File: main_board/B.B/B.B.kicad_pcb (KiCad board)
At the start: 4 copper layers, 196 x 98 mm, 254 parts, among them J2 Conn_01x11, J3 Conn_01x11, J5 USB_C_Receptacle_USB2.0, M1 Motor_DC, Q1 2N7002, Q10 2N7002, Q11 SI3447CDV, Q2 2N7002, Q3 AO3400A, Q5 SI3447CDV, Q7 SI3447CDV, Q8 2N7002, Q9 SI3447CDV, SW1 SW_DIP_x01, SW2 SW_DIP_x01, SW3 SW_DIP_x01, SW4 SW_DIP_x02, U1 WS2812, U10 WS2812, U11 WS2812, U12 WS2812, U13 WS2812, U14 WS2812, U15 WS2812, U16 WS2812, U17 WS2812, U18 WS2812, U19 WS2812, U2 WS2812, U20 WS2812, U21 WS2812, U22 WS2812, U23 WS2812, U24 WS2812, U25 WS2812, U26 WS2812, U27 WS2812, U28 WS2812, U29 WS2812, U3 WS2812, U30 WS2812, U31 WS2812, U32 WS2812, U33 WS2812, U34 WS2812, U35 WS2812, U36 WS2812, U37 WS2812, U38 WS2812, U39 WS2812, U4 WS2812, U40 WS2812, U41 WS2812, U42 WS2812, U43 WS2812, U44 WS2812, U45 WS2812, U46 WS2812, U47 WS2812, U48 WS2812, U49 WS2812, U5 WS2812, U50 WS2812, U51 WS2812, U52 WS2812, U53 WS2812, U54 WS2812, U55 WS2812, U56 WS2812, U57 WS2812, U58 WS2812, U59 WS2812, U6 WS2812, U60 WS2812, U61 BMX055, U62 AOZ1280, U63 FP6276, U64 CP2102N-A01-GQFN28, U65 ESP32-WROVER, U66 LDC1314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

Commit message: uvolneni enkoderu
- dolomitelny enkoder
- zmenseni via u civek LDC
- vymena pouzdra USB-C
- otoceni IR prijmace
- zakas vylivani medi pod BMX9555
- odstraneni "ochrannych" odporu k M41T62
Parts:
- removed C105: 0.1uf, Capacitor_SMD:C_0805_2012Metric
- removed C106: 10uf, Capacitor_SMD:C_0805_2012Metric
- removed R39, R9: 220, Resistor_SMD:R_0402_1005Metric
- added J1: Conn_01x04, Connector_PinSocket_2.54mm:PinSocket_1x04_P2.54mm_Vertical, F.Cu at (182.9, 57.1)
- added J4: Conn_01x04, Connector_PinSocket_2.54mm:PinSocket_1x04_P2.54mm_Vertical, F.Cu at (190.4, 57.2)
- J5: footprint Connector_USB:USB_C_Receptacle_Amphenol_12401610E4-2A -> BB:USB_C_Female-16Pin-HPJF
- moved C87 12.5 mm to (226.4, 85.5), turned to 180 degrees
- moved C75 10.6 mm to (216.2, 79.5), turned to 0 degrees
- moved C90 7.88 mm to (234.5, 93.9), turned to 270 degrees
- moved C81 7.33 mm to (200.3, 104.9), turned to 270 degrees
- moved C93 6.39 mm to (216.2, 81.5), turned to 0 degrees
- moved R46 5.99 mm to (192.7, 63.8)
- moved U70 5.98 mm to (195.1, 63.8)
- moved C71 5.98 mm to (194.5, 61.5)
- moved C72 5.98 mm to (194.5, 66.2)
- moved C74 5.98 mm to (194.5, 60.0)
- moved R47 5.98 mm to (192.7, 57.7)
- moved U71 5.98 mm to (195.1, 57.7)
- moved C73 5.98 mm to (194.5, 55.4)
- moved D2 5.90 mm to (205.0, 103.5)
- moved C102 5.89 mm to (169.0, 113.3), turned to 270 degrees
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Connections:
- C71 pad 1: +3V3 -> Net-(C71-Pad1)
- C71 pad 2: GND -> Net-(C71-Pad2)
- C72 pad 1: /expanz00/ENC_OUT_0 -> Net-(C72-Pad1)
- C72 pad 2: GND -> Net-(C71-Pad2)
- C73 pad 1: +3V3 -> Net-(C71-Pad1)
- C73 pad 2: GND -> Net-(C71-Pad2)
- C74 pad 1: /expanz00/ENC_OUT_1 -> Net-(C74-Pad1)
- C74 pad 2: GND -> Net-(C71-Pad2)
- J2 pad 6: /ESP3200/IO19 -> /ESP3200/IO18
- J2 pad 7: /ESP3200/IO18 -> /ESP3200/IO19
- Q3 pad 1: Net-(C105-Pad1) -> Net-(Q3-Pad1)
- R28 pad 1: Net-(C105-Pad1) -> Net-(Q3-Pad1)
- R46 pad 1: +3V3 -> Net-(C71-Pad1)
- R46 pad 2: /expanz00/ENC_OUT_0 -> Net-(C72-Pad1)
- R47 pad 1: +3V3 -> Net-(C71-Pad1)
- R47 pad 2: /expanz00/ENC_OUT_1 -> Net-(C74-Pad1)
- SW4 pad 3: Net-(C105-Pad1) -> Net-(Q3-Pad1)
- U64 pad 8: Net-(C105-Pad1) -> Net-(C102-Pad1)
- U67 pad 10: Net-(R39-Pad1) -> /ESP3200/IO22
- U67 pad 9: Net-(R9-Pad1) -> /ESP3200/IO23
- U70 pad 1: +3V3 -> Net-(C71-Pad1)
- U70 pad 2: /expanz00/ENC_OUT_0 -> Net-(C72-Pad1)
- U70 pad 3: GND -> Net-(C71-Pad2)
- U71 pad 1: +3V3 -> Net-(C71-Pad1)
- U71 pad 2: /expanz00/ENC_OUT_1 -> Net-(C74-Pad1)
- U71 pad 3: GND -> Net-(C71-Pad2)
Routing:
- net Net-(C71-Pad2): track 0.00 -> 23.9 mm, vias 0 -> 4
- net VCC: track 55.0 -> 76.3 mm, vias 2 -> 4
- net Net-(C105-Pad1): track 17.9 -> 0.00 mm, vias 2 -> 0
- net Net-(C71-Pad1): track 0.00 -> 16.4 mm
- net Net-(C74-Pad1): track 0.00 -> 10.7 mm, vias 0 -> 1
- net /ESP3200/IO23: track 91.5 -> 101.8 mm
- net /ESP3200/D+: track 16.3 -> 26.1 mm, vias 0 -> 2
- net /ESP3200/IO19: track 66.6 -> 75.9 mm
- net /expanz00/ENC_OUT_1: track 94.0 -> 85.4 mm, vias 4 -> 3
- net /ESP3200/5V_USB: track 130.5 -> 122.1 mm
- net Net-(Q3-Pad1): track 0.00 -> 7.71 mm
- net /ESP3200/IO15-up: track 30.9 -> 24.1 mm, vias 2 -> 0
- net Net-(C72-Pad1): track 0.00 -> 6.43 mm
- net /ESP3200/IO2-down: track 37.2 -> 30.9 mm, vias 2 -> 0
- net /ESP3200/IO5-up: track 55.8 -> 49.6 mm
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- added copper zone on F.Cu, net Net-(C85-Pad1)
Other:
- outline, holes or cut-outs redrawn

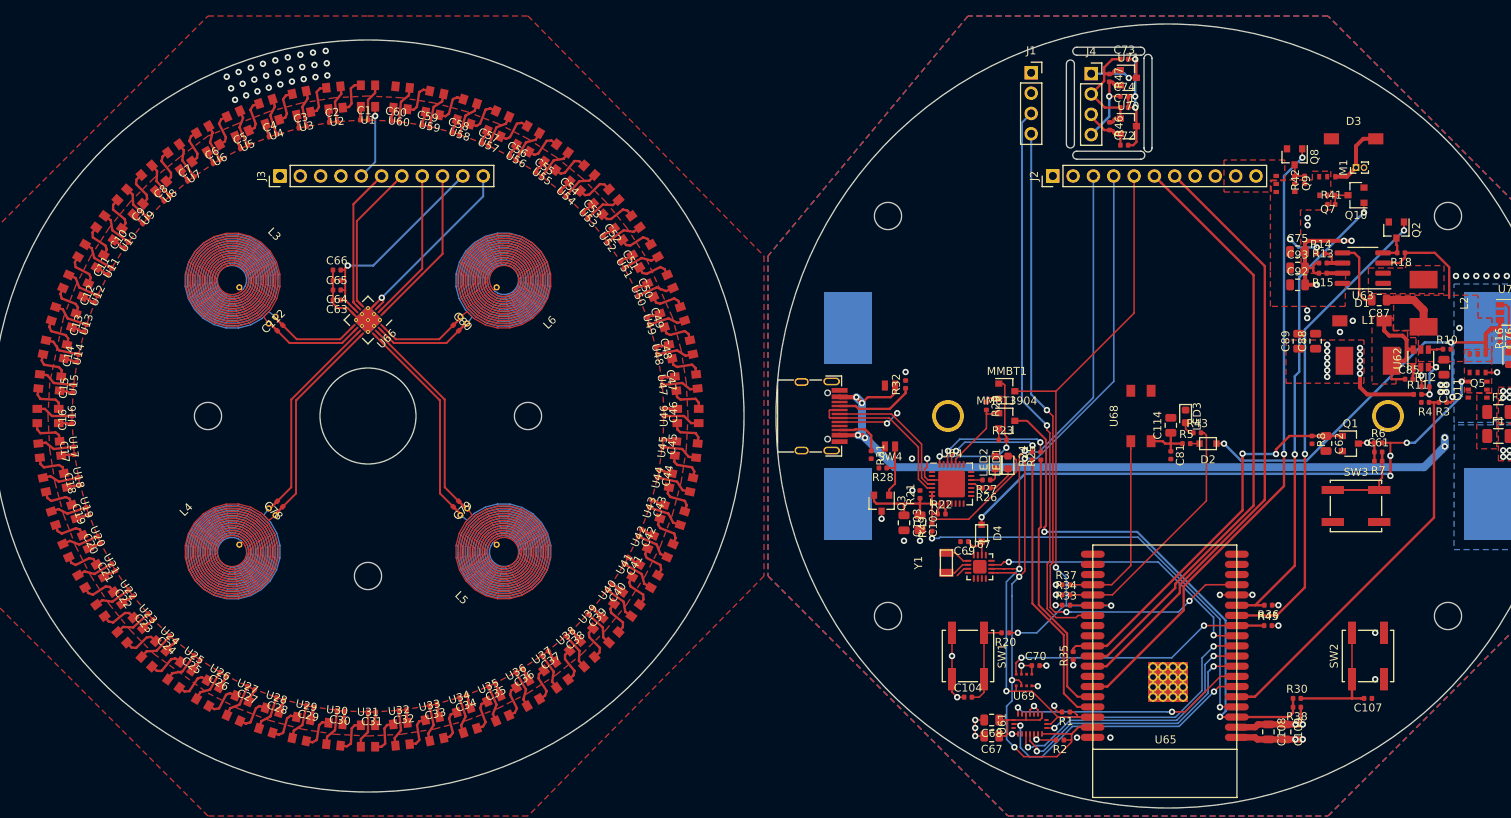
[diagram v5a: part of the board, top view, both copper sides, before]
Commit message: popisky
-popisky
-poladeni uddeleni enkoderu
-poladeni nayvu drah
-priopjeni gnd USB
-poligon V5 na led-desce do spodni vrstvu
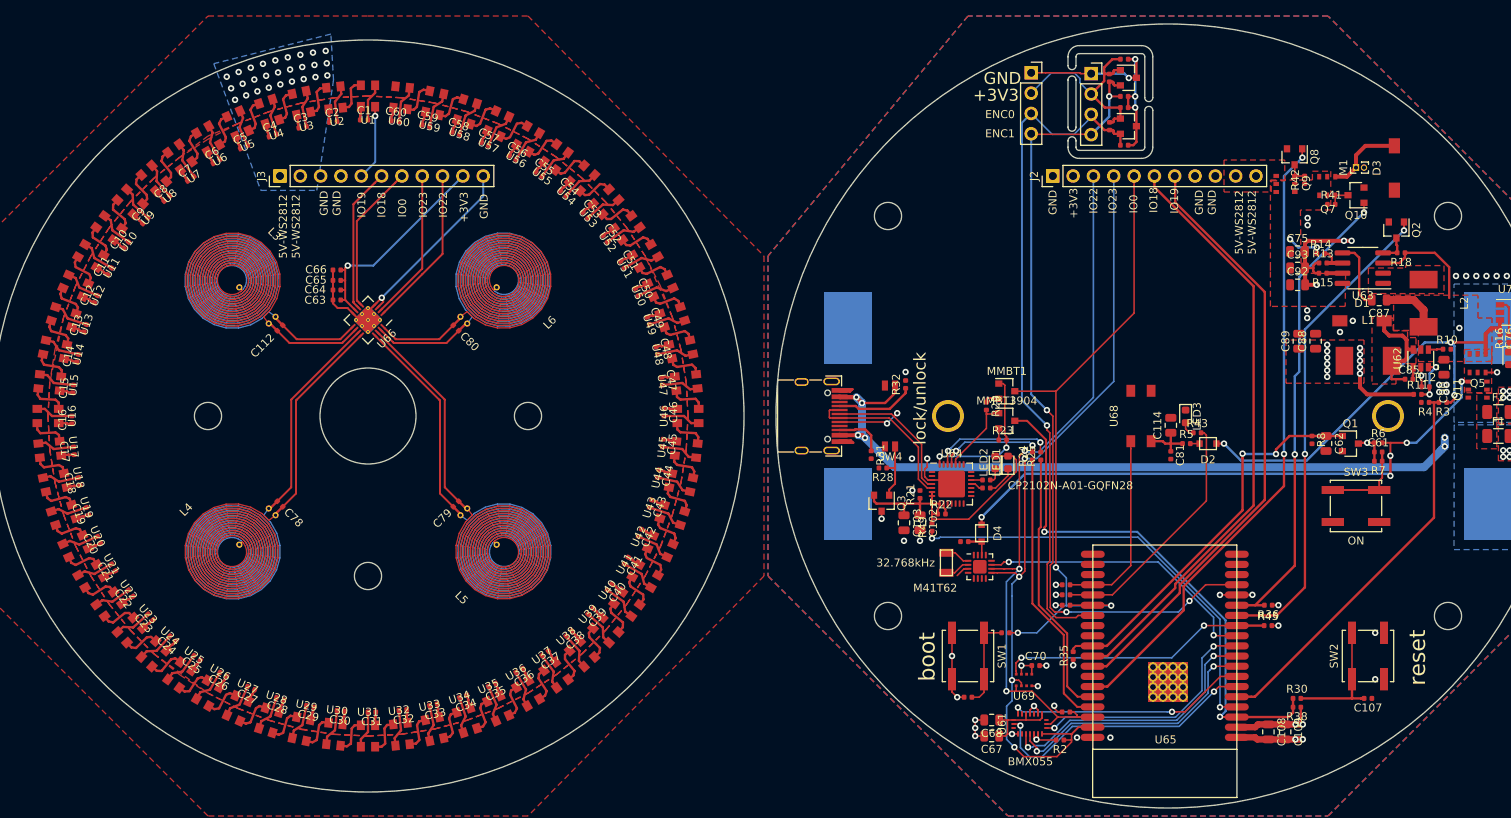
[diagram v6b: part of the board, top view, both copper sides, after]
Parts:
- moved D3 6.27 mm to (228.3, 69.0), turned to 270 degrees
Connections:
- C71 pad 1: Net-(C71-Pad1) -> +3V3
- C71 pad 2: Net-(C71-Pad2) -> GND
- C72 pad 1: Net-(C72-Pad1) -> /expanz00/ENC_OUT_0
- C72 pad 2: Net-(C71-Pad2) -> GND
- C73 pad 1: Net-(C71-Pad1) -> +3V3
- C73 pad 2: Net-(C71-Pad2) -> GND
- C74 pad 1: Net-(C74-Pad1) -> /expanz00/ENC_OUT_1
- C74 pad 2: Net-(C71-Pad2) -> GND
- J4 pad 1: Net-(C71-Pad2) -> GND
- J4 pad 2: Net-(C71-Pad1) -> +3V3
- J4 pad 3: Net-(C72-Pad1) -> /expanz00/ENC_OUT_0
- J4 pad 4: Net-(C74-Pad1) -> /expanz00/ENC_OUT_1
- R46 pad 1: Net-(C71-Pad1) -> +3V3
- R46 pad 2: Net-(C72-Pad1) -> /expanz00/ENC_OUT_0
- R47 pad 1: Net-(C71-Pad1) -> +3V3
- R47 pad 2: Net-(C74-Pad1) -> /expanz00/ENC_OUT_1
- U70 pad 1: Net-(C71-Pad1) -> +3V3
- U70 pad 2: Net-(C72-Pad1) -> /expanz00/ENC_OUT_0
- U70 pad 3: Net-(C71-Pad2) -> GND
- U71 pad 1: Net-(C71-Pad1) -> +3V3
- U71 pad 2: Net-(C74-Pad1) -> /expanz00/ENC_OUT_1
- U71 pad 3: Net-(C71-Pad2) -> GND
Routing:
- net GND: track 67.3 -> 106.1 mm, vias 45 -> 49
- net +3V3: track 42.6 -> 69.3 mm
- net Net-(C71-Pad2): track 23.9 -> 0.00 mm, vias 4 -> 0
- net /expanz00/ENC_OUT_1: track 85.4 -> 103.7 mm, vias 3 -> 4
- net /expanz00/ENC_OUT_0: track 70.2 -> 86.9 mm
- net Net-(C71-Pad1): track 16.4 -> 0.00 mm
- net Net-(C74-Pad1): track 10.7 -> 0.00 mm, vias 1 -> 0
- net Net-(C72-Pad1): track 6.43 -> 0.00 mm
- net Net-(D3-Pad1): track 8.60 -> 9.90 mm
- net Net-(C69-Pad1): track 3.89 -> 3.37 mm
- added copper zone on B.Cu, net /next-board00/5V
- removed copper zone on In1.Cu, net /next-board00/5V
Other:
- outline, holes or cut-outs redrawn
- board text added: "+"
- board text added: "+3V3"
- board text added: "-"
- board text added: "5V-WS2812 5V-WS2812"
- board text added: "ENC0"
- board text added: "ENC1"
- board text added: "GND"
- board text added: "GND GND"
- board text added: "IO0"
- board text added: "IO18"
- board text added: "IO19"
- board text added: "IO22"
- board text added: "IO23"
- board text added: "ON"
- board text added: "boot"
- board text added: "lock/unlock"
- board text added: "reset"

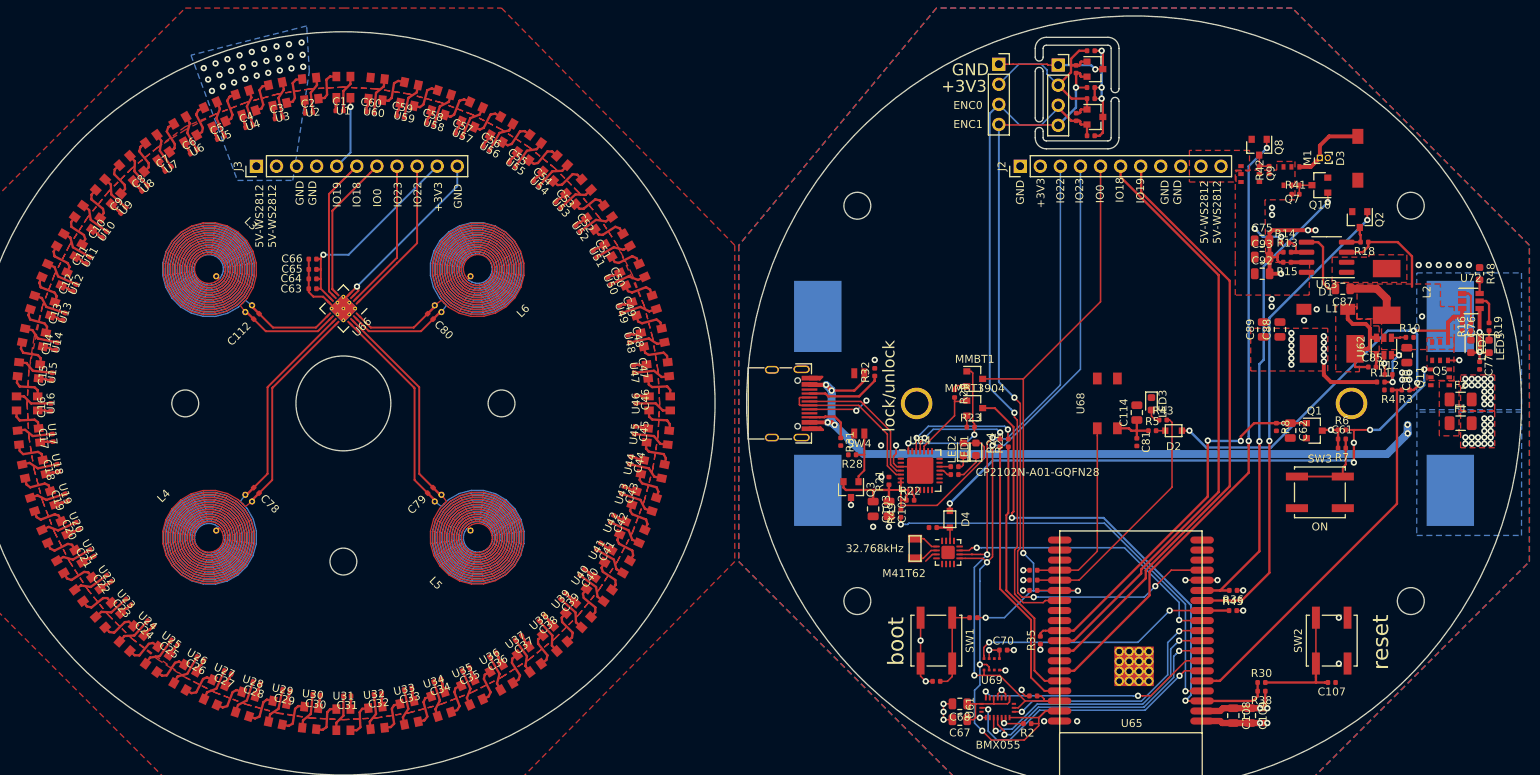
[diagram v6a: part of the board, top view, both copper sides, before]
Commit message: LDC footprint
prodlouzeni pedu pro usnadneni rucniho osazovani
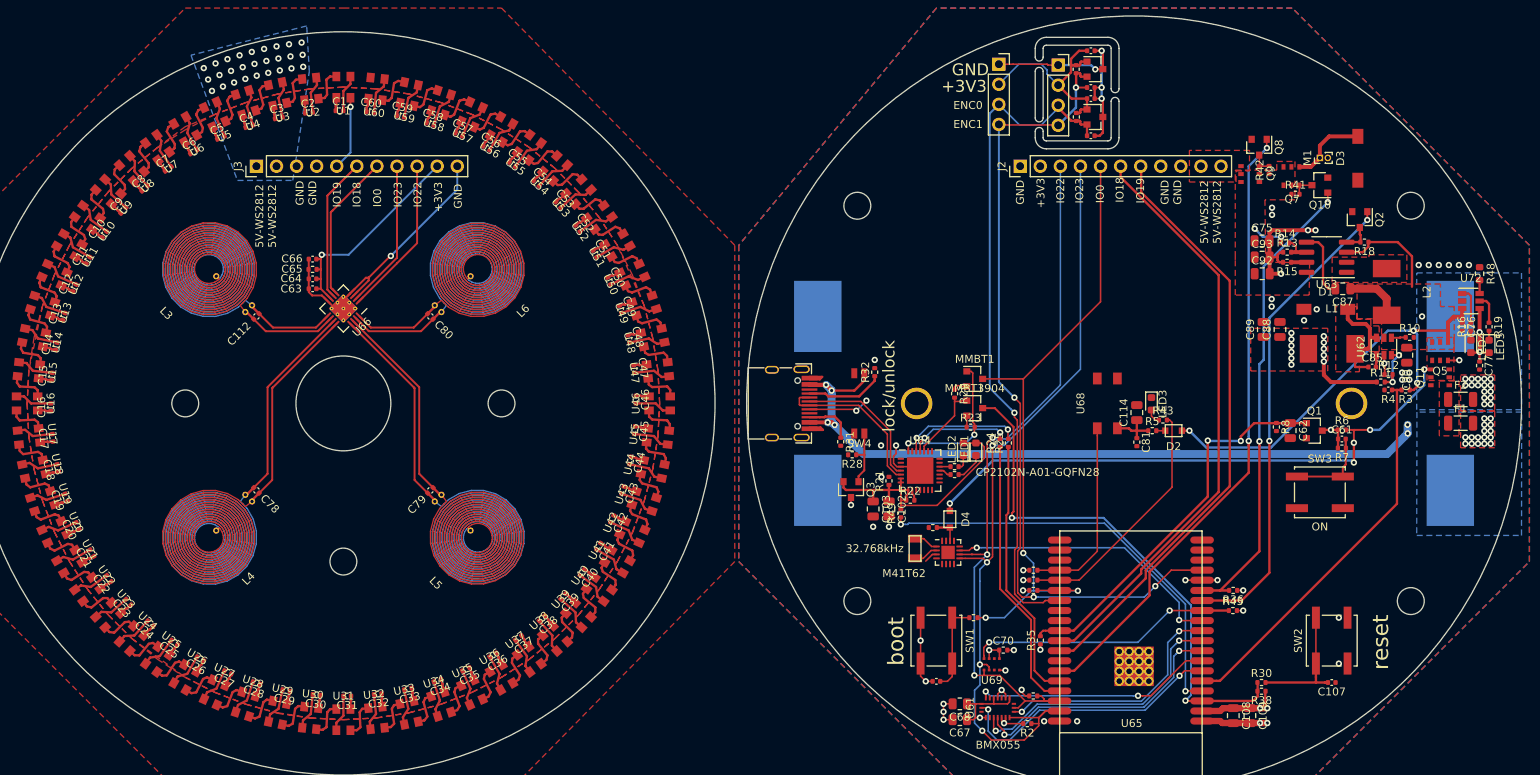
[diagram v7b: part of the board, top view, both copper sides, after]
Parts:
- U66: footprint Package_DFN_QFN:WQFN-16-1EP_4x4mm_P0.5mm_EP2.6x2.6mm_ThermalVias -> BB:WQFN-16_4x4mm
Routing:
- net /next-board00/LDC-GND: track 37.6 -> 39.5 mm

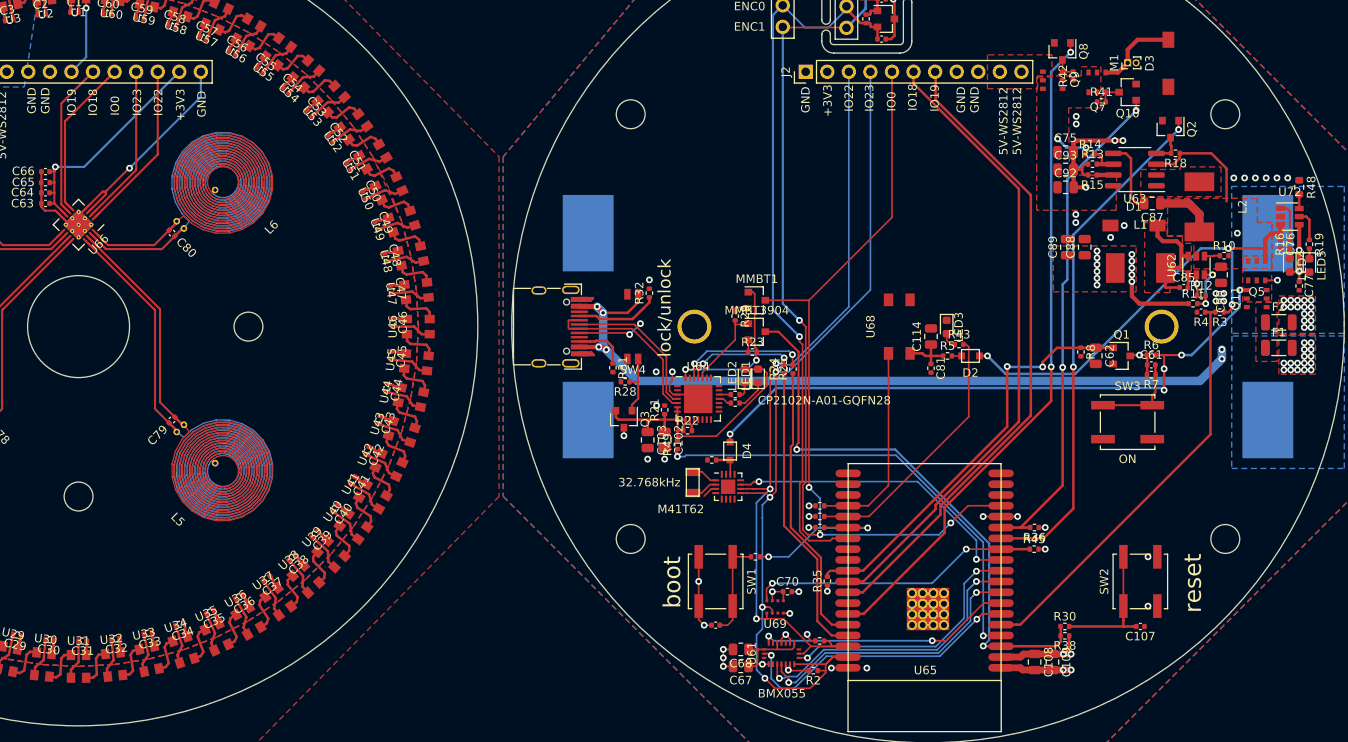
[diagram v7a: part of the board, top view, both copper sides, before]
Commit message: JLCdata
- korekce pozice a natoceni
- data pro vyrobu
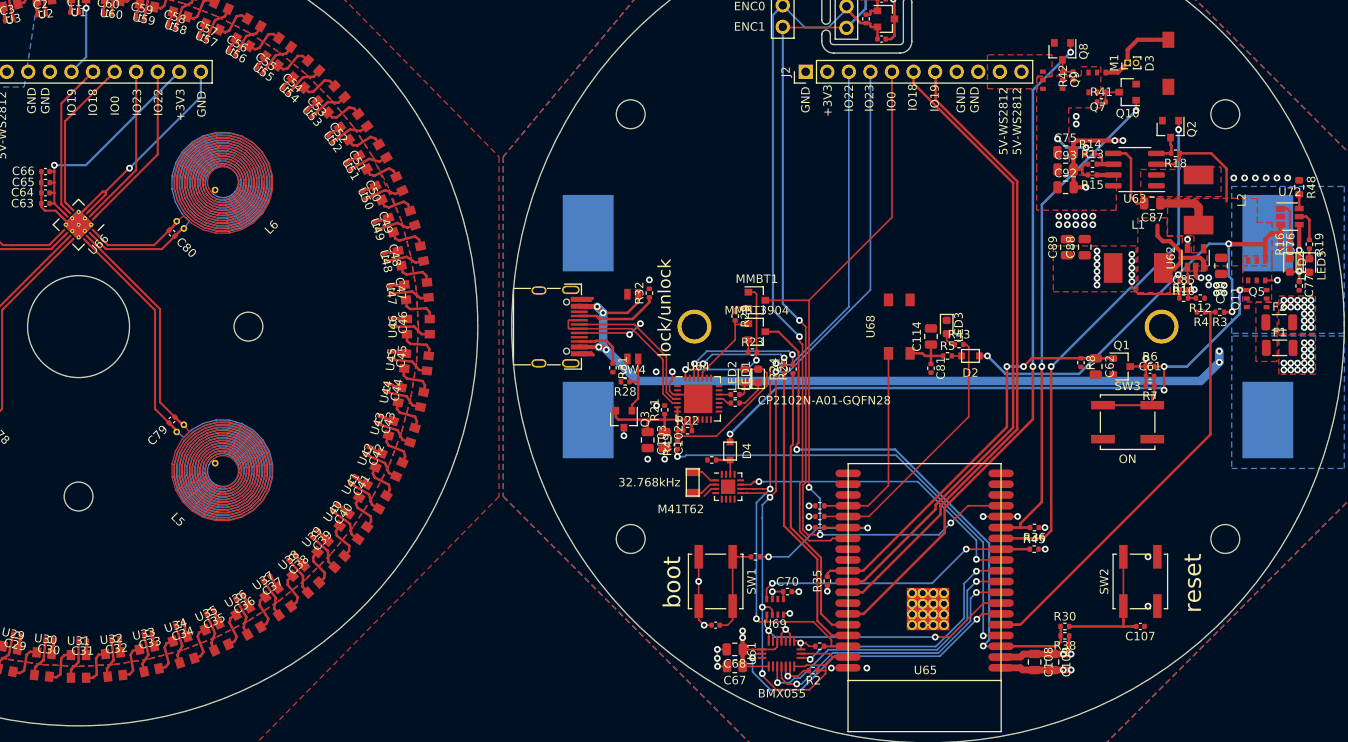
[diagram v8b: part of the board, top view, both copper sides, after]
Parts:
- removed D1: SS54, BB:DO-214AC
- C68: footprint Resistor_SMD:R_0805_2012Metric -> Capacitor_SMD:C_0805_2012Metric
- C85: value 10nf -> 22nf
- U62: value AOZ1280 -> SY8009; footprint Package_TO_SOT_SMD:SOT-23-6 -> Package_TO_SOT_SMD:SOT-23-5
- U66: footprint BB:WQFN-16_4x4mm -> Package_DFN_QFN:WQFN-16-1EP_4x4mm_P0.5mm_EP2.6x2.6mm_ThermalVias
- moved R10 5.63 mm to (230.1, 94.7), turned to 180 degrees
- moved R6 1.36 mm to (226.1, 104.7)
- moved C61 1.36 mm to (226.1, 105.8)
- moved R7 1.36 mm to (226.1, 107.0)
- moved R11 1.28 mm to (230.1, 96.7)
- moved C62 1.25 mm to (219.8, 104.7)
- moved Q1 1.25 mm to (222.8, 104.7)
- moved R8 1.25 mm to (218.0, 104.2)
- moved C90 1.05 mm to (234.5, 92.8)
- moved U62 0.91 mm to (231.5, 91.9)
- moved L2 0.81 mm to (231.8, 85.1)
- moved C68 0.71 mm to (177.2, 138.0)
- moved C67 0.70 mm to (177.3, 140.0)
- moved R1 0.63 mm to (187.2, 137.6)
- moved R12 0.33 mm to (232.1, 96.7), turned to 180 degrees
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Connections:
- C85 pad 1: Net-(C85-Pad1) -> +3V3
- L1 pad 1: Net-(C85-Pad1) -> Net-(L1-Pad1)
- R11 pad 2: Net-(R11-Pad2) -> Net-(C85-Pad2)
- R12 pad 2: Net-(R11-Pad2) -> Net-(C85-Pad2)
- U62 pad 1: Net-(C85-Pad2) -> Net-(R10-Pad1)
- U62 pad 3: Net-(R11-Pad2) -> Net-(L1-Pad1)
- U62 pad 4: Net-(R10-Pad1) -> VCC
- U62 pad 5: VCC -> Net-(C85-Pad2)
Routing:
- net Net-(C85-Pad1): track 13.5 -> 0.00 mm
- net Net-(L1-Pad1): track 0.00 -> 11.9 mm
- net Net-(C85-Pad2): track 1.52 -> 9.78 mm, vias 0 -> 2
- net Net-(R11-Pad2): track 6.68 -> 0.00 mm, vias 2 -> 0
- net +3V3: track 69.3 -> 73.2 mm, vias 21 -> 22
- net /ESP3200/IO23: track 101.8 -> 105.5 mm
- net /ESP3200/IO34: track 34.8 -> 36.8 mm
- net VCC: track 76.4 -> 78.1 mm
- net /ESP3200/IO22: track 89.7 -> 88.1 mm
- net Net-(C61-Pad2): track 10.7 -> 9.33 mm
- net /ESP3200/IO19: track 75.9 -> 74.6 mm
- net /ESP3200/IO33: track 34.6 -> 35.5 mm
- net /ESP3200/IO5-up: track 49.6 -> 48.7 mm
- net /ESP3200/IO18: track 74.6 -> 74.0 mm
- net /ESP3200/IO35: track 30.2 -> 30.8 mm
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- added copper zone on F.Cu, net Net-(L1-Pad1)
- removed copper zone on F.Cu, net Net-(C85-Pad1)
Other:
- rule via_min_size: 0.4 -> 0.35
